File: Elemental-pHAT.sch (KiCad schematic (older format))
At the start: 44 parts

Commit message: CVPCB y netlist finished
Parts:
- removed J?: Jack-DC, symbol Jack-DC
- added C1, C4: 22uF, Capacitors_Tantalum_SMD:CP_Tantalum_Case-A_EIA-3216-18_Hand, symbol CP_Small
- added C2, C3: 100nF, Capacitors_SMD:C_0805_HandSoldering, symbol C_Small
- added D1: LED_PURPLE, LEDs:LED_0805_HandSoldering, symbol LED_Small
- added J10: USB, Connectors_USB:USB_Micro-B_Molex-105017-0001, symbol USB_A
- added J14: JP_3.3V, Pin_Headers:Pin_Header_Straight_1x03_Pitch2.54mm, symbol Conn_01x03_Male
- added J21: JP_5V, Pin_Headers:Pin_Header_Straight_1x03_Pitch2.54mm, symbol Conn_01x03_Male
- added R1: 1k, Resistors_SMD:R_0805_HandSoldering, symbol R_Small
- added U2: AMS1117, SOT223, symbol V_REG_LM1117SOT223
- C5: renamed from C?; footprint (none) -> Capacitors_THT:CP_Radial_D8.0mm_P3.80mm
- J1, J11, J12, J13, J15, J16, J17, J2, J3, J4, J5, J6, J7, J8, J9: renamed from J?; footprint (none) -> Pin_Headers:Pin_Header_Straight_1x03_Pitch2.54mm
- J18: renamed from J?; value Conn_01x01 -> CH5; footprint (none) -> Connectors_TestPoints:Test_Point_Pad_d1.5mm
- J19: renamed from J?; value Conn_01x01 -> CH6; footprint (none) -> Connectors_TestPoints:Test_Point_Pad_d1.5mm
- J20: renamed from J?; value Conn_01x01 -> CH7; footprint (none) -> Connectors_TestPoints:Test_Point_Pad_d1.5mm
- J22, J23: renamed from J?; footprint (none) -> Connectors_JST:JST_PH_S4B-PH-K_04x2.00mm_Angled
- J24: renamed from J?; value Conn_01x01 -> SER6; footprint (none) -> Connectors_TestPoints:Test_Point_Pad_d1.5mm
- J25: renamed from J?; value Conn_01x01 -> SER7; footprint (none) -> Connectors_TestPoints:Test_Point_Pad_d1.5mm
- J26: renamed from J?; value Conn_01x01 -> SER8; footprint (none) -> Connectors_TestPoints:Test_Point_Pad_d1.5mm
- J27: renamed from J?; value Conn_01x01 -> SER9; footprint (none) -> Connectors_TestPoints:Test_Point_Pad_d1.5mm
- J28: renamed from J?; value Conn_01x01 -> SER10; footprint (none) -> Connectors_TestPoints:Test_Point_Pad_d1.5mm
- J29: renamed from J?; value Conn_01x01 -> SER11; footprint (none) -> Connectors_TestPoints:Test_Point_Pad_d1.5mm
- JP1, JP2, JP3, JP4, JP5, JP6: renamed from JP?; footprint (none) -> conn-test:JUMPER-SOLDER-SMD
- R2, R3, R4, R5, R6, R7, R8: renamed from R?; footprint (none) -> Resistors_SMD:R_0805_HandSoldering
- U1: renamed from U?; footprint (none) -> kicad_componentes:z_RPiZero_Hat_NPTH
- U4: renamed from U?; footprint (none) -> Housings_SOIC:SOIC-16_3.9x9.9mm_Pitch1.27mm
- gave numbers to parts that had none: 1
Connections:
- net +3V3: now also J14.2 (Pin_2); no longer U1.1 (3.3V), U1.17 (3.3V)
- net +5V: now also J21.2 (Pin_2), R1.1
- net GND: now also C1.2, C2.2, C3.2, C4.2, D1.1 (K), J10.4 (GND), J10.5 (Shield), U2.1 (ADJ)
- net 5VRPI: now reaches U1.2 (5V)
- net 5VRPI: now also U1.4 (5V), J21.1 (Pin_1)
- new net: D1.2 (A), R1.2
- new net 3V3RPI: J14.1 (Pin_1), U1.1 (3.3V), U1.17 (3.3V)
- new net 3V3USB: C3.1, C4.1, J14.3 (Pin_3), U2.2 (OUT), U2.4 (OUT)
- new net 5VUSB: C1.1, C2.1, J10.1 (VBUS), J21.3 (Pin_3), U2.3 (IN)
- no-connect marks 0 -> 19

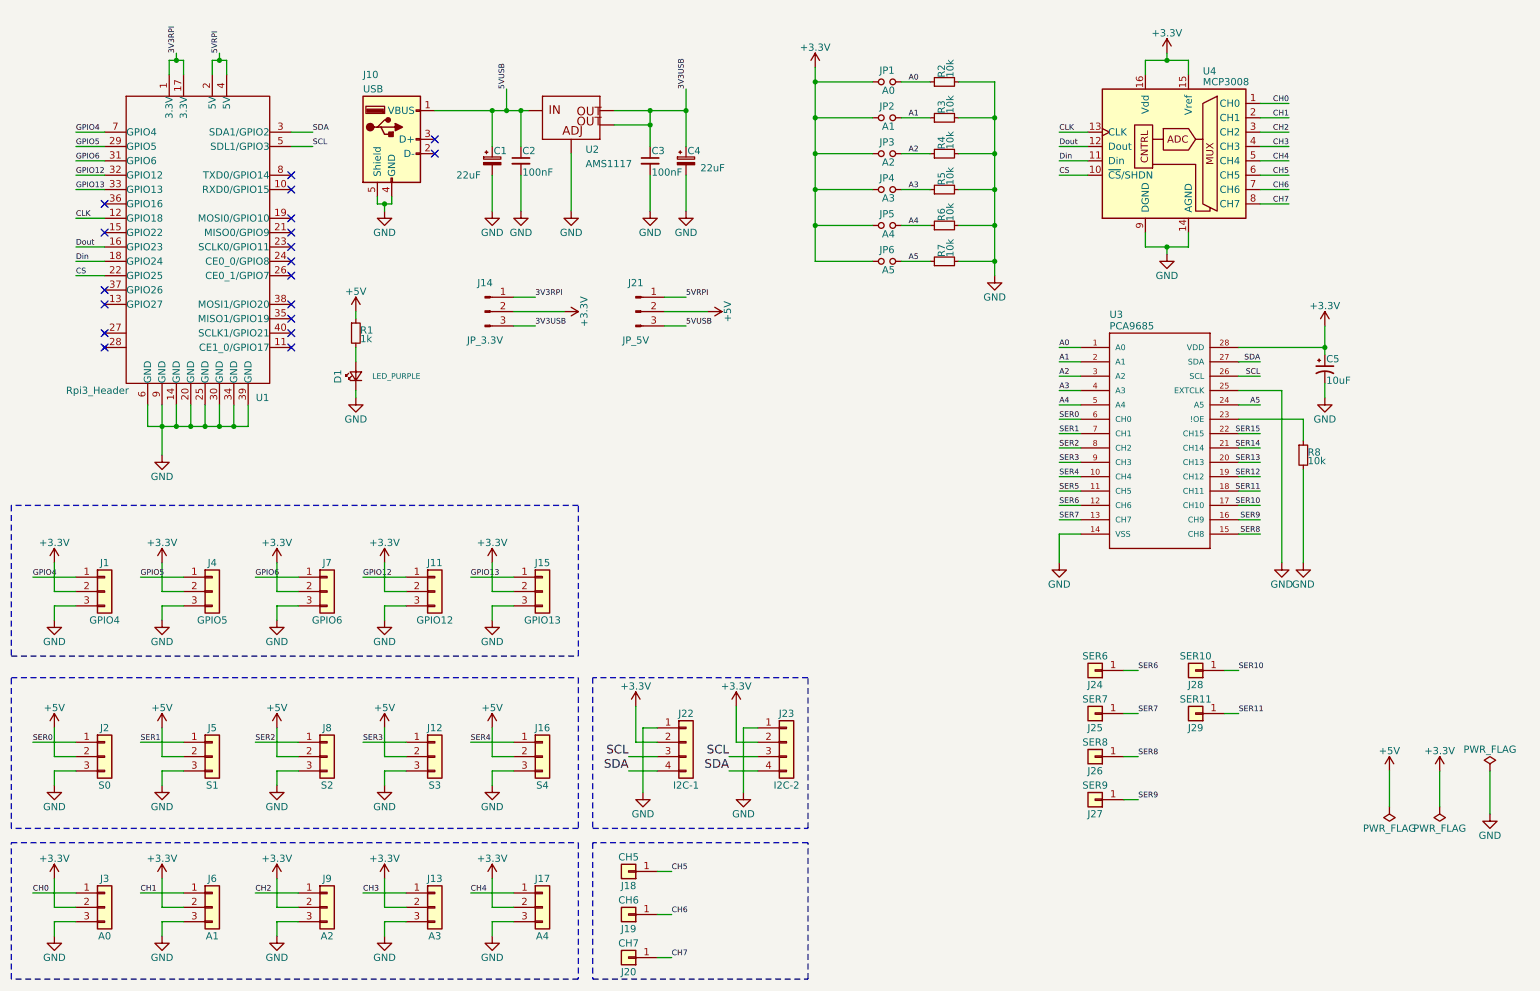
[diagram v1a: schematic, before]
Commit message: Extra pads deleted
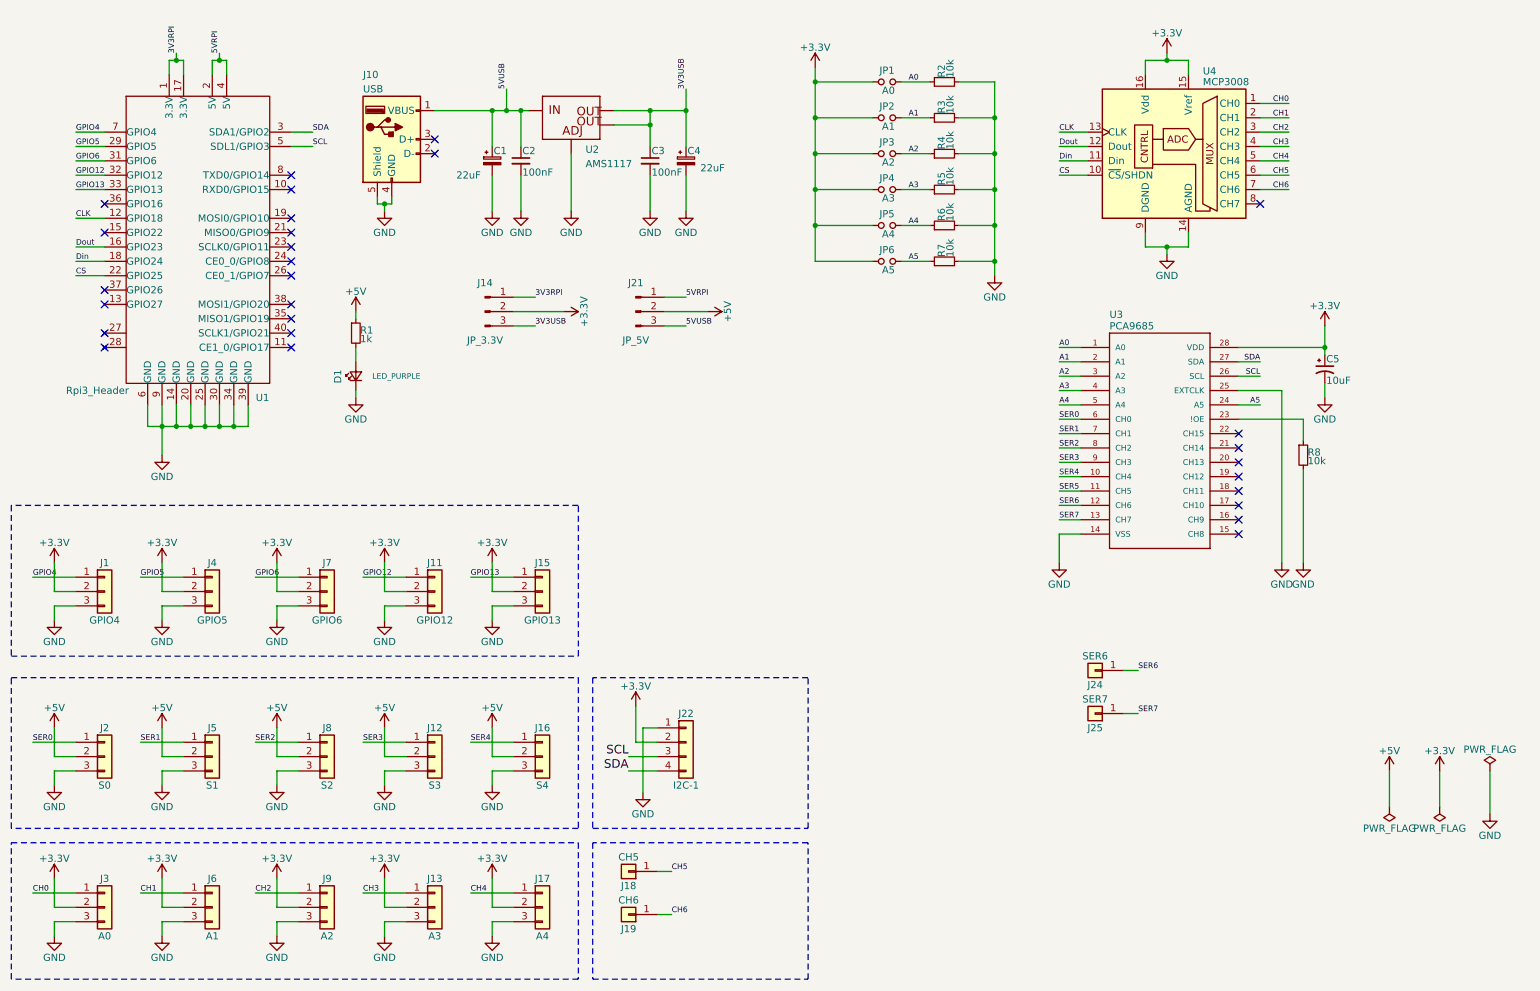
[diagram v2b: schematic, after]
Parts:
- removed J20: CH7, Connectors_TestPoints:Test_Point_Pad_d1.5mm, symbol Conn_01x01
- removed J23: I2C-2, Connectors_JST:JST_PH_S4B-PH-K_04x2.00mm_Angled, symbol Conn_01x04
- removed J26: SER8, Connectors_TestPoints:Test_Point_Pad_d1.5mm, symbol Conn_01x01
- removed J27: SER9, Connectors_TestPoints:Test_Point_Pad_d1.5mm, symbol Conn_01x01
- removed J28: SER10, Connectors_TestPoints:Test_Point_Pad_d1.5mm, symbol Conn_01x01
- removed J29: SER11, Connectors_TestPoints:Test_Point_Pad_d1.5mm, symbol Conn_01x01
- U2: footprint SOT223 -> TO_SOT_Packages_SMD:SOT-223
- U3: footprint TSSOP-28_4MM -> Housings_SSOP:TSSOP-28_4.4x9.7mm_Pitch0.65mm
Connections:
- net CH7: no longer names the net of U4.8 (CH7)
- net SER10: no longer names the net of U3.17 (CH10)
- net SER11: no longer names the net of U3.18 (CH11)
- net SER12: no longer names the net of U3.19 (CH12)
- net SER13: no longer names the net of U3.20 (CH13)
- net SER14: no longer names the net of U3.21 (CH14)
- net SER15: no longer names the net of U3.22 (CH15)
- net SER8: no longer names the net of U3.15 (CH8)
- net SER9: no longer names the net of U3.16 (CH9)
- no-connect marks 19 -> 28
